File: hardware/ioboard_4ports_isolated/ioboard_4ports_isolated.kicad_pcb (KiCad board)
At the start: 2 copper layers, 106 x 55 mm, 58 parts, among them J1 Conn_02x06_Odd_Even, J10 XLR3, J11 XLR3, J12 Conn_01x03, J13 Conn_01x03, J2 XLR3, J3 XLR3, J4 XLR3, J5 XLR3, J6 Conn_01x03, J7 Conn_01x03, J8 XLR3, J9 XLR3, U1 M24C02-WMN, U2 CRE1S0505DC, U3 CRE1S0505DC, U4 ADM2483xRW, U5 ADM2483xRW, U6 ADM2483xRW, U7 ADM2483xRW

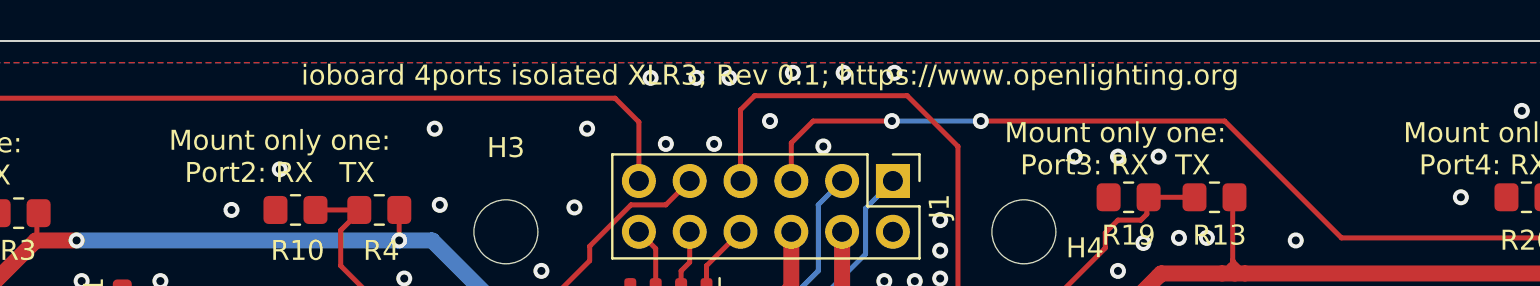
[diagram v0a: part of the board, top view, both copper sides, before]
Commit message: Unify board naming and bump all to rev 0.2
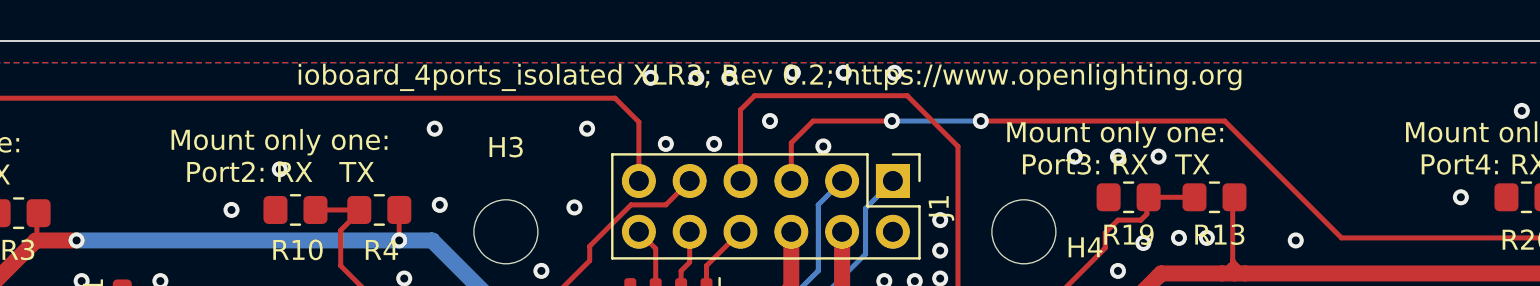
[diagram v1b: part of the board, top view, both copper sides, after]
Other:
- board text added: "ioboard_4ports_isolated XLR3; Rev 0.2; https://www.openlighting.org"
- board text removed: "ioboard 4ports isolated XLR3; Rev 0.1; https://www.openlighting.org"
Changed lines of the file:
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@@
   (page A4)
   (title_block
-    (title "rp2040_dongle ioboard 4slots cheap")
-    (date 2021-03-21)
-    (rev 0.1)
+    (title rp2040_dongle_ioboard_4ports_isolated)
+    (date 2021-03-28)
+    (rev 0.2)
     (company https://www.openlighting.org)
   )
@@
     (effects (font (size 1 1) (thickness 0.15)))
   )
-  (gr_text "ioboard 4ports isolated XLR3; Rev 0.1; https://www.openlighting.org" (at 78.105 21.717) (layer F.SilkS)
+  (gr_text "ioboard_4ports_isolated XLR3; Rev 0.2; https://www.openlighting.org" (at 78.105 21.717) (layer F.SilkS)
     (effects (font (size 1 1) (thickness 0.15)))
   )

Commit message: Hardware: Make the reference path to the library relative and save the files with the new kicad version
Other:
- net class Default removed

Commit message: Finish IO-Board updates
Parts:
- U1: value M24C02-WMN -> M24C64-RMN6TP
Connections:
- U4 pad 10: (no net) -> unconnected-(U4-Pad10)
- U4 pad 11: (no net) -> unconnected-(U4-Pad11)
- U4 pad 14: (no net) -> unconnected-(U4-Pad14)
- U5 pad 10: (no net) -> unconnected-(U5-Pad10)
- U5 pad 11: (no net) -> unconnected-(U5-Pad11)
- U5 pad 14: (no net) -> unconnected-(U5-Pad14)
- U6 pad 10: (no net) -> unconnected-(U6-Pad10)
- U6 pad 11: (no net) -> unconnected-(U6-Pad11)
- U6 pad 14: (no net) -> unconnected-(U6-Pad14)
- U7 pad 10: (no net) -> unconnected-(U7-Pad10)
- U7 pad 11: (no net) -> unconnected-(U7-Pad11)
- U7 pad 14: (no net) -> unconnected-(U7-Pad14)
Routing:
- net +3V3: track 180.0 -> 178.8 mm
- net /GND_3+4: vias 59 -> 47
- net /GND_1+2: vias 50 -> 49
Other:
- board text added: "ioboard_4ports_isolated XLR3; Rev 0.5; https://github.com/OpenLightingProject/rp2040-dmxsun"
- board text removed: "ioboard_4ports_isolated XLR3; Rev 0.2; https://www.openlighting.org"

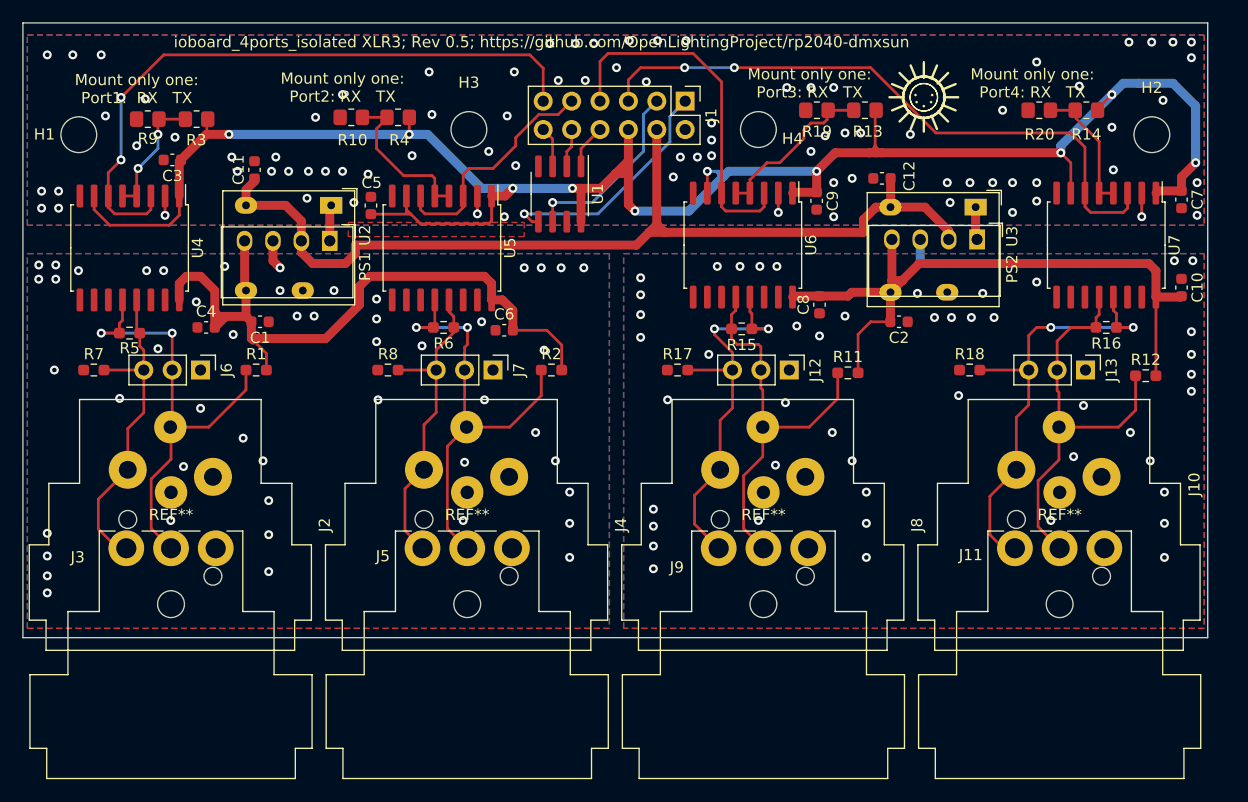
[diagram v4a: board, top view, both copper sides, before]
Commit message: Add RJ45 jack to ioboard_4ports_isolated as well
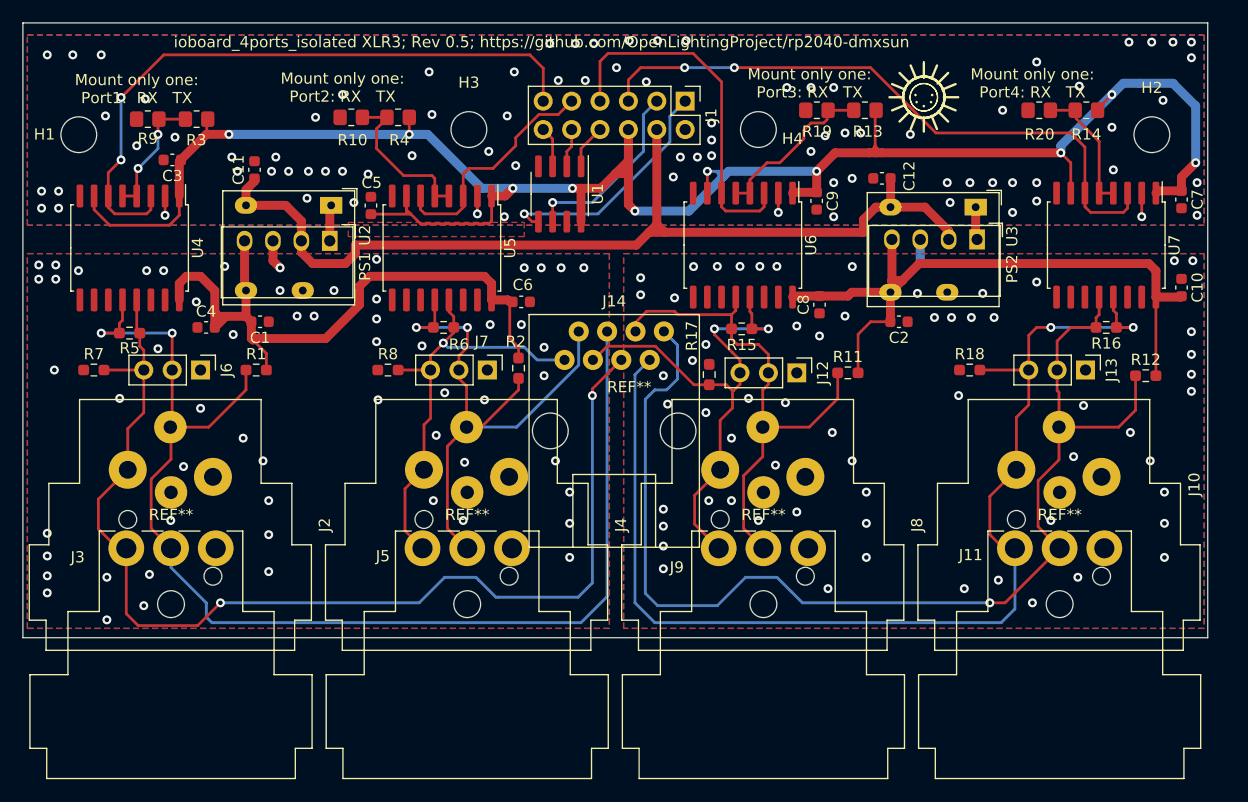
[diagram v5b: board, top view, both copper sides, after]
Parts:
- added J14: 8P8C, RJ45_Sparkfun:RJ45_Sparkfun, F.Cu at (77.9, 56.5)
- moved C6 2.96 mm to (69.6, 45.0), turned to 180 degrees
- moved R2 2.95 mm to (69.3, 50.9), turned to 90 degrees
- moved R17 2.86 mm to (86.4, 51.5), turned to -90 degrees
- moved J12 0.72 mm to (94.2, 51.3)
- moved J7 0.51 mm to (66.5, 51.1)
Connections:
- net Net-(J10-Pad2) renamed /RJ45_OUT_7
- net Net-(J10-Pad3) renamed /RJ45_OUT_8
- net Net-(J12-Pad2) renamed /RJ45_OUT_6
- net Net-(J12-Pad3) renamed /RJ45_OUT_5
- net Net-(J2-Pad2) renamed /RJ45_OUT_2
- net Net-(J2-Pad3) renamed /RJ45_OUT_1
- net Net-(J4-Pad2) renamed /RJ45_OUT_3
- net Net-(J4-Pad3) renamed /RJ45_OUT_4
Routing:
- net /RJ45_OUT_2: track 29.2 -> 101.3 mm, vias 0 -> 2
- net /RJ45_OUT_1: track 41.7 -> 109.9 mm
- net /RJ45_OUT_8: track 37.6 -> 104.9 mm, vias 0 -> 1
- net /RJ45_OUT_7: track 40.4 -> 103.3 mm
- net /RJ45_OUT_4: track 40.1 -> 53.1 mm
- net /RJ45_OUT_3: track 28.3 -> 39.7 mm, vias 0 -> 1
- net /RJ45_OUT_5: track 35.8 -> 47.2 mm
- net /RJ45_OUT_6: track 36.4 -> 46.8 mm
- net /VBUS_1+2: track 63.1 -> 59.0 mm
- net /GND_3+4: vias 47 -> 61
- net /GND_1+2: vias 49 -> 58

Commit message: Bump all boards to rev 0.6
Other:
- board text added: "ioboard_4ports_isolated XLR3; Rev 0.6; https://github.com/OpenLightingProject/rp2040-dmxsun"
- board text removed: "ioboard_4ports_isolated XLR3; Rev 0.5; https://github.com/OpenLightingProject/rp2040-dmxsun"
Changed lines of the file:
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@@
     (effects (font (size 1 1) (thickness 0.15)))
   )
-  (gr_text "ioboard_4ports_isolated XLR3; Rev 0.5; https://github.com/OpenLightingProject/rp2040-dmxsun" (at 71.4 21.717) (layer "F.SilkS")
+  (gr_text "ioboard_4ports_isolated XLR3; Rev 0.6; https://github.com/OpenLightingProject/rp2040-dmxsun" (at 71.4 21.717) (layer "F.SilkS")
     (effects (font (size 1 1) (thickness 0.15)))
   )
